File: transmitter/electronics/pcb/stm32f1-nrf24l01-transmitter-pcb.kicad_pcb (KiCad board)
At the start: 2 copper layers, 128 x 47 mm, 79 parts, among them J1 PA1/A1, J10 PB3, J11 PB4, J12 PB5, J13 PB6, J14 PB7, J15 PB8, J16 PB10, J17 PB11, J18 External charger LED, J19 BATTERY, J2 PA2/A2, J20 Red, J21 Blue, J22 POWER SWITCH, J23 USB, J24 UART, J25 SWD, J26 Buzzer, J27 NRF24 connector, J29 Meter, J3 PA3/A3, J30 LED, J4 PA4/A4, J5 PA5/A5, J6 PA6/A6, J7 PA7/A7, J8 PB0/A8, J9 PB1/A9, Q1 PMV30UN, SW1 RESET, U1 MCP1703A-3302, U2 LIPO_CHARGER_+_PROTECTION, U3 STM32F103CBT6, U4 MCP1703A-3302, Y1 8MHz

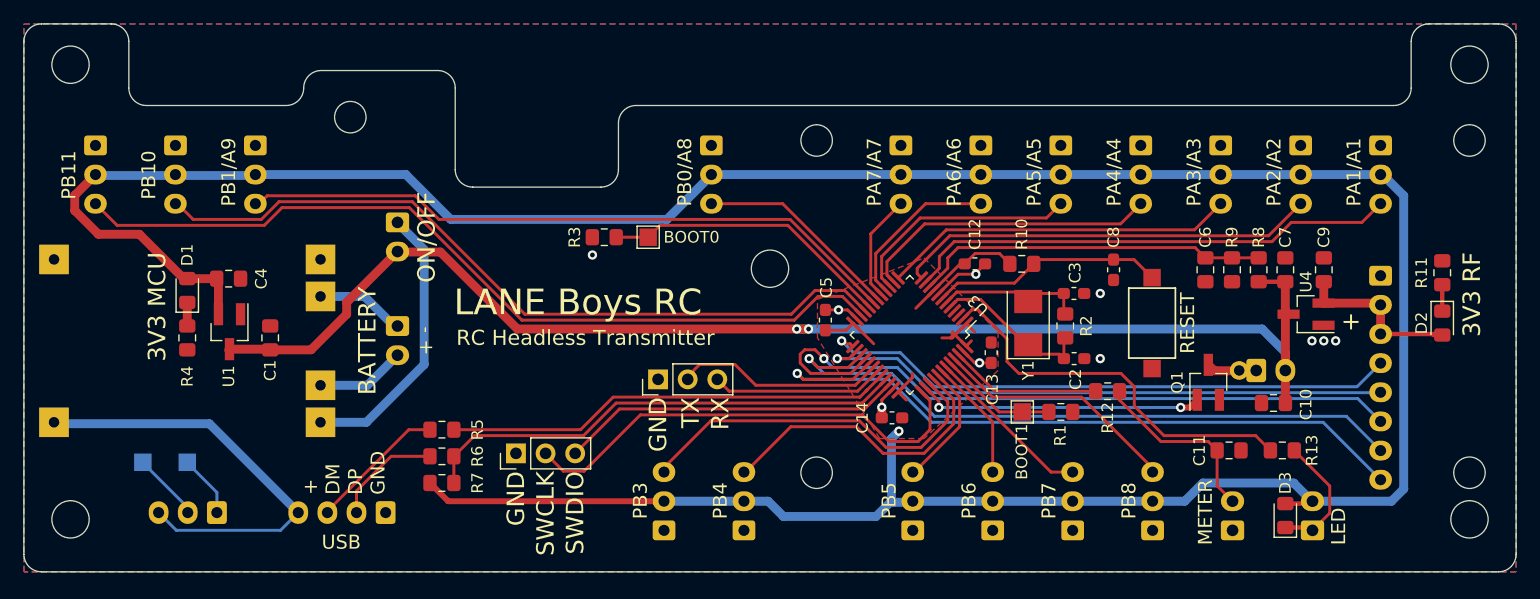
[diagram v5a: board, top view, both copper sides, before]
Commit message: More layout improvements
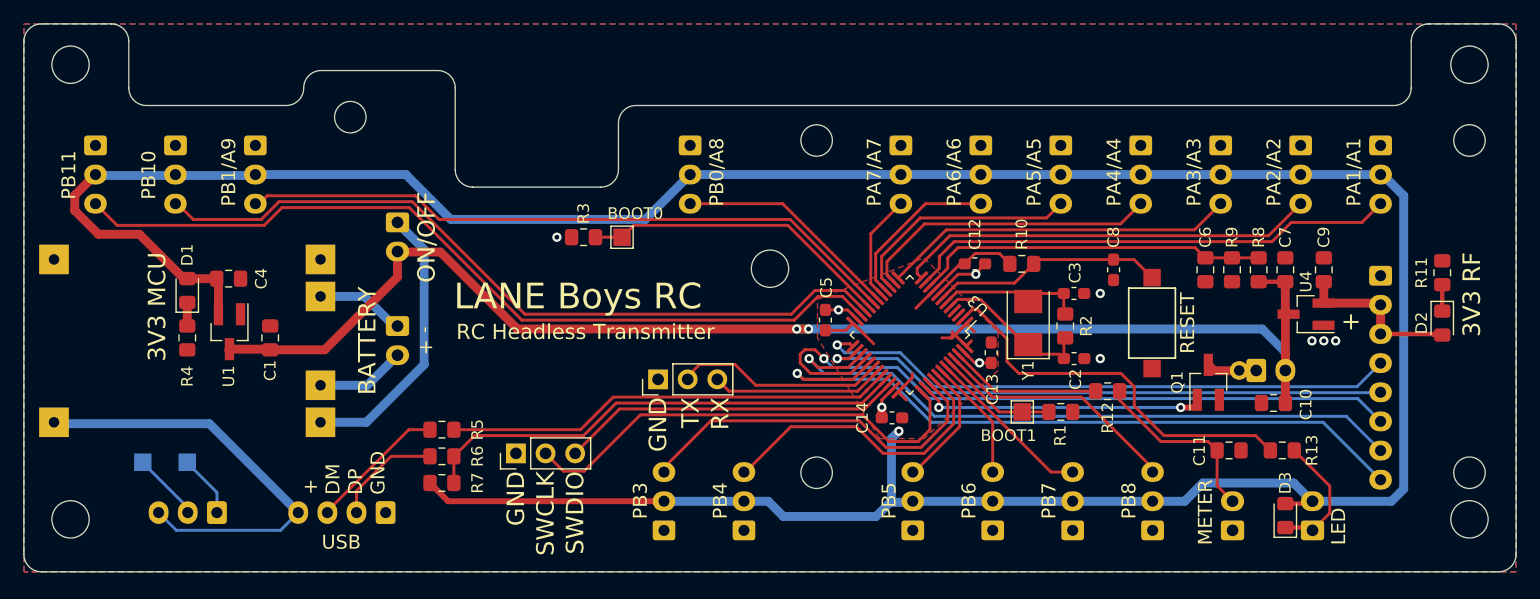
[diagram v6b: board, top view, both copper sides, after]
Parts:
- moved TP2 2.24 mm to (122.3, 71.3)
- moved J8 1.82 mm to (128.2, 63.4)
- moved R3 1.78 mm to (119.0, 71.3)
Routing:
- net /BOOT1: track 25.0 -> 27.1 mm
- net /PB0-ADC8: track 17.6 -> 19.4 mm
- net VDD: track 113.7 -> 114.4 mm
- net /CSN: track 49.9 -> 50.4 mm

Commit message: Tweak MCU power supply
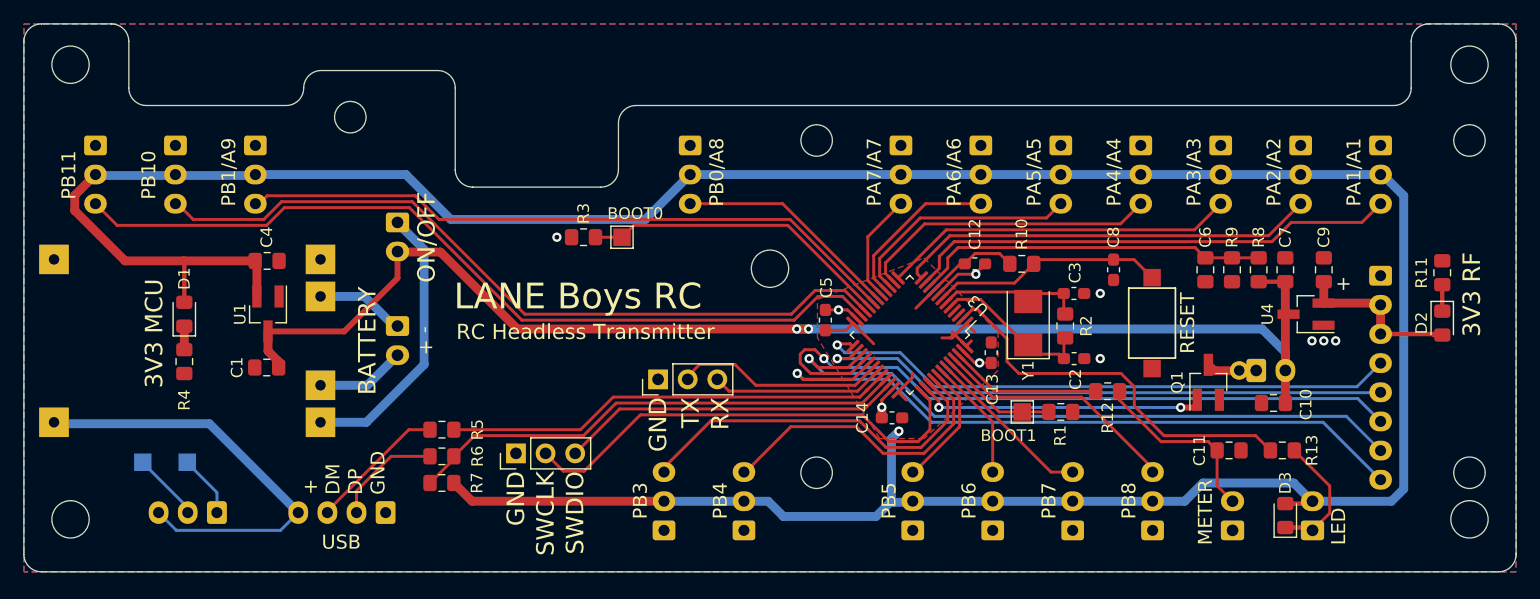
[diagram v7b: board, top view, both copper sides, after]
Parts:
- moved U1 3.64 mm to (91.9, 77.9)
- moved C4 3.64 mm to (91.9, 73.3)
- moved C1 2.56 mm to (91.8, 82.5), turned to 180 degrees
- moved D1 2.05 mm to (84.8, 77.9)
- moved R4 2.05 mm to (84.8, 82.0)
- turned R7 to 180 degrees
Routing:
- net +3V3: track 284.9 -> 289.1 mm
- net /USBDP: track 42.1 -> 42.9 mm
- net VDD: track 114.4 -> 113.9 mm
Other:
- net class Default: clearance 0.1524 -> 0.1778
- rule trace_clearance: 0.1524 -> 0.1778

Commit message: Improve layout, ready for manufacturing
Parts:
- moved R12 10.5 mm to (173.1, 89.6)
- moved J24 3.51 mm to (128.9, 83.5)
- moved C11 3.05 mm to (177.4, 89.6)
- moved R13 2.79 mm to (181.7, 89.6)
- moved J25 1.73 mm to (114.9, 89.8)
- moved R5 0.25 mm to (107.1, 87.8)
- moved R6 0.25 mm to (107.1, 90.1)
- moved R7 0.25 mm to (107.1, 92.4)
- moved C14 0.21 mm to (145.7, 86.8)
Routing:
- net /METER: track 13.3 -> 24.3 mm
- net Net-(C11-Pad1): track 15.9 -> 6.96 mm
- net /TX: track 18.0 -> 14.3 mm
- net /RX: track 14.9 -> 11.4 mm
- net +3V3: track 289.1 -> 292.2 mm
- net /LED: track 33.8 -> 36.5 mm
- net /SWDCLK: track 40.5 -> 38.6 mm
- net /SWDIO: track 29.5 -> 28.0 mm
- net Net-(D3-Pad1): track 11.5 -> 10.4 mm
- net Net-(J23-Pad3): track 12.1 -> 12.6 mm
- net GND: track 15.0 -> 15.1 mm, vias 10 -> 11
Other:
- board text added: "+ Red Blue"
